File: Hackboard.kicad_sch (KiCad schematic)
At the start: 15 parts, among them SW1 SW_MEC_5E, U1 STM32L476RGT6

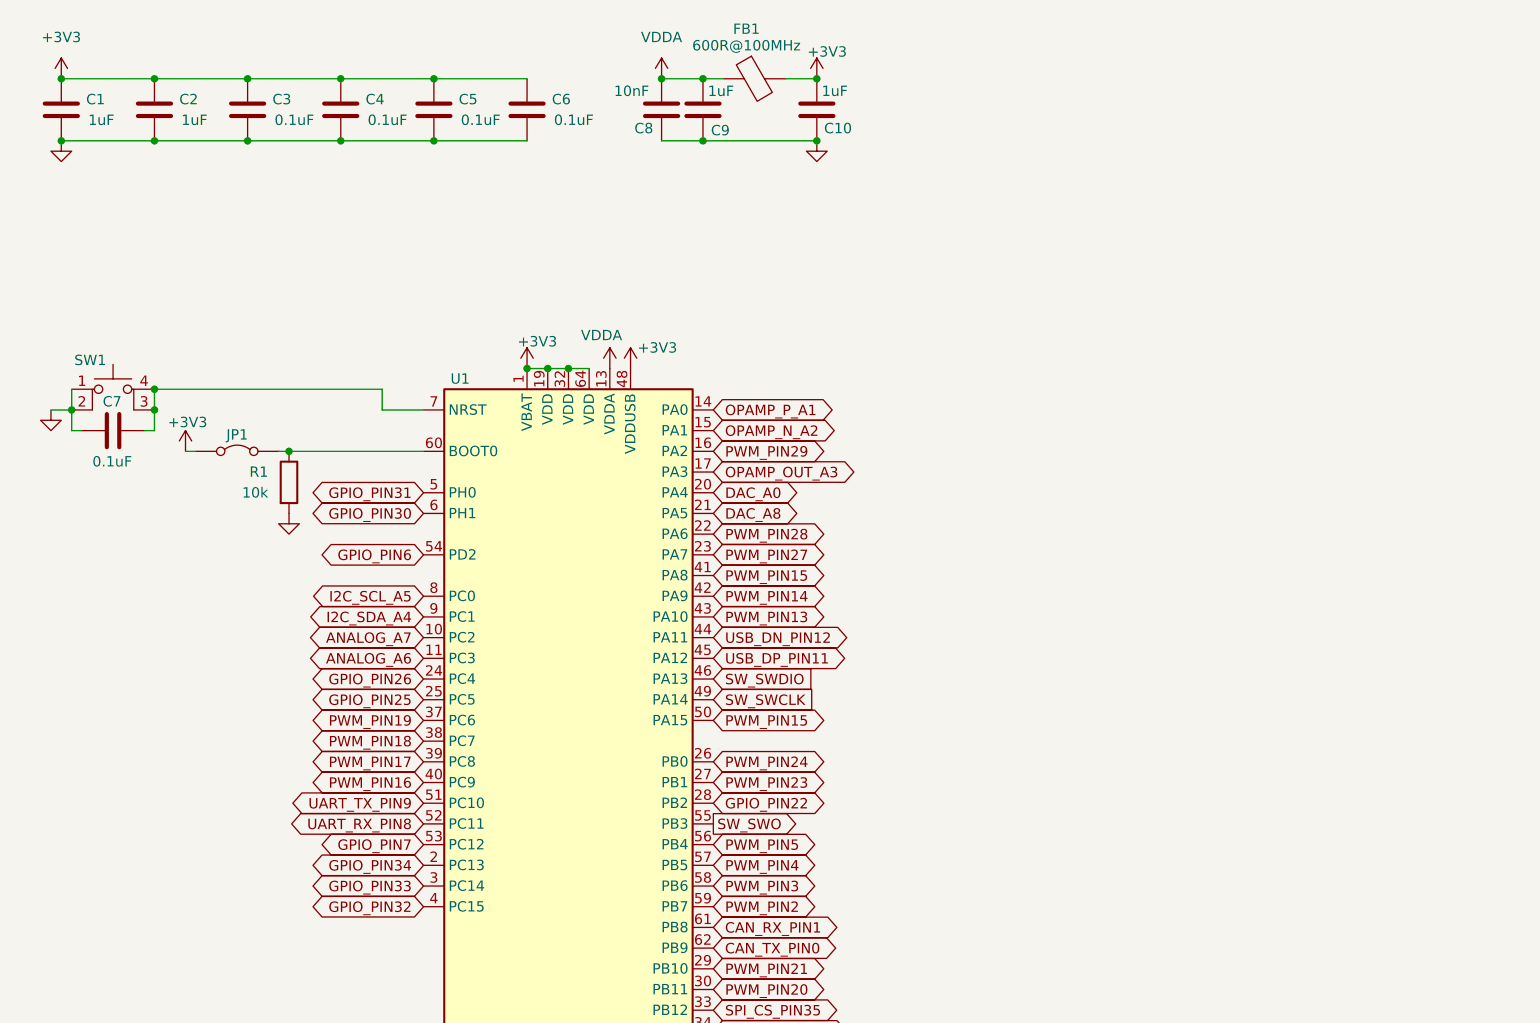
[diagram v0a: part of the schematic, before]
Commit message: Update README; Add power line and SPI for Micro SD
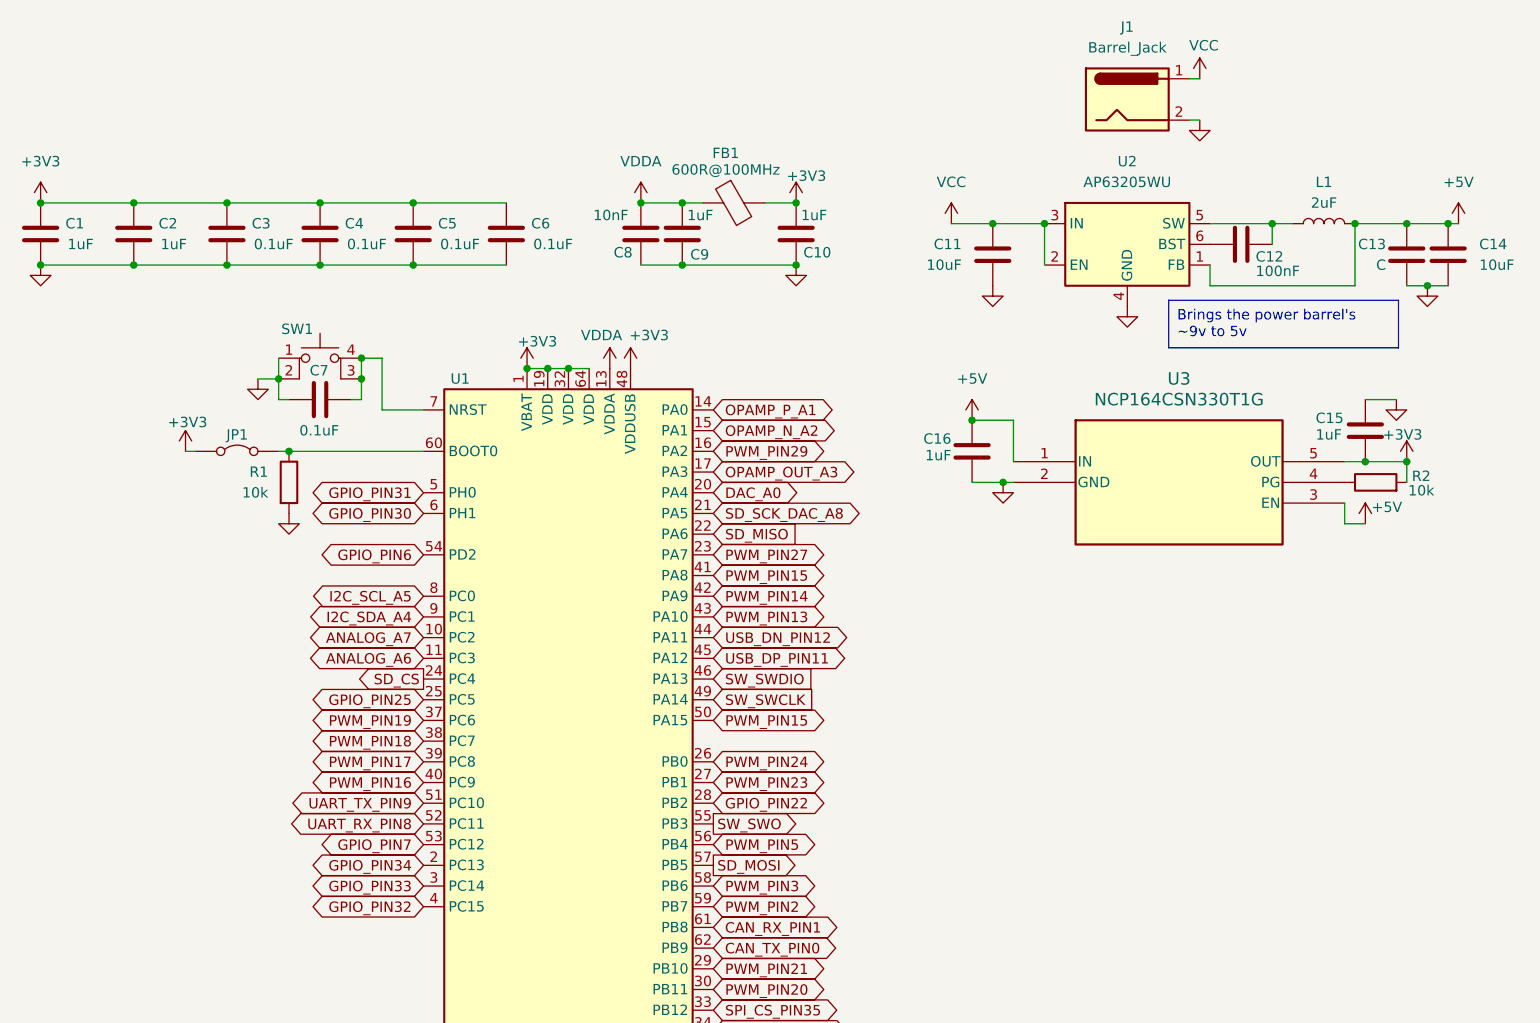
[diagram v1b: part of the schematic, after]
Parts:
- added C11, C14: 10uF, symbol Device:C
- added C12: 100nF, symbol Device:C
- added C13: C, symbol Device:C
- added C15, C16: 1uF, symbol Device:C
- added J1: Barrel_Jack, symbol Connector:Barrel_Jack
- added L1: 2uF, symbol Device:L
- added R2: 10k, symbol Device:R
- added U2: AP63205WU, Package_TO_SOT_SMD:TSOT-23-6, symbol Regulator_Switching:AP63205WU
- added U3: NCP164CSN330T1G, FP-NCP164CSN330T1G_OSI, symbol NCP164CSN:NCP164CSN330T1G
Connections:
- net +3V3: now also C15.2, R2.2, U3.5 (OUT)
- net GND: now also C11.2, C13.2, C14.2, C15.1, C16.2, J1.2, U2.4 (GND), U3.2 (GND)
- net DAC_A8 renamed SD_SCK_DAC_A8
- net GPIO_PIN26 renamed SD_CS
- net PWM_PIN28 renamed SD_MISO
- net PWM_PIN4 renamed SD_MOSI
- new net: C12.2, L1.1, U2.5 (SW)
- new net: R2.1, U3.4 (PG)
- new net: C12.1, U2.6 (BST)
- new net +5V: C13.1, C14.1, C16.1, L1.2, U2.1 (FB), U3.1 (IN), U3.3 (EN)
- new net VCC: C11.1, J1.1, U2.2 (EN), U2.3 (IN)
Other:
- moved on the sheet: C1, C10, C2, C3, C4, C5, C6, C7, C8, C9, FB1, SW1

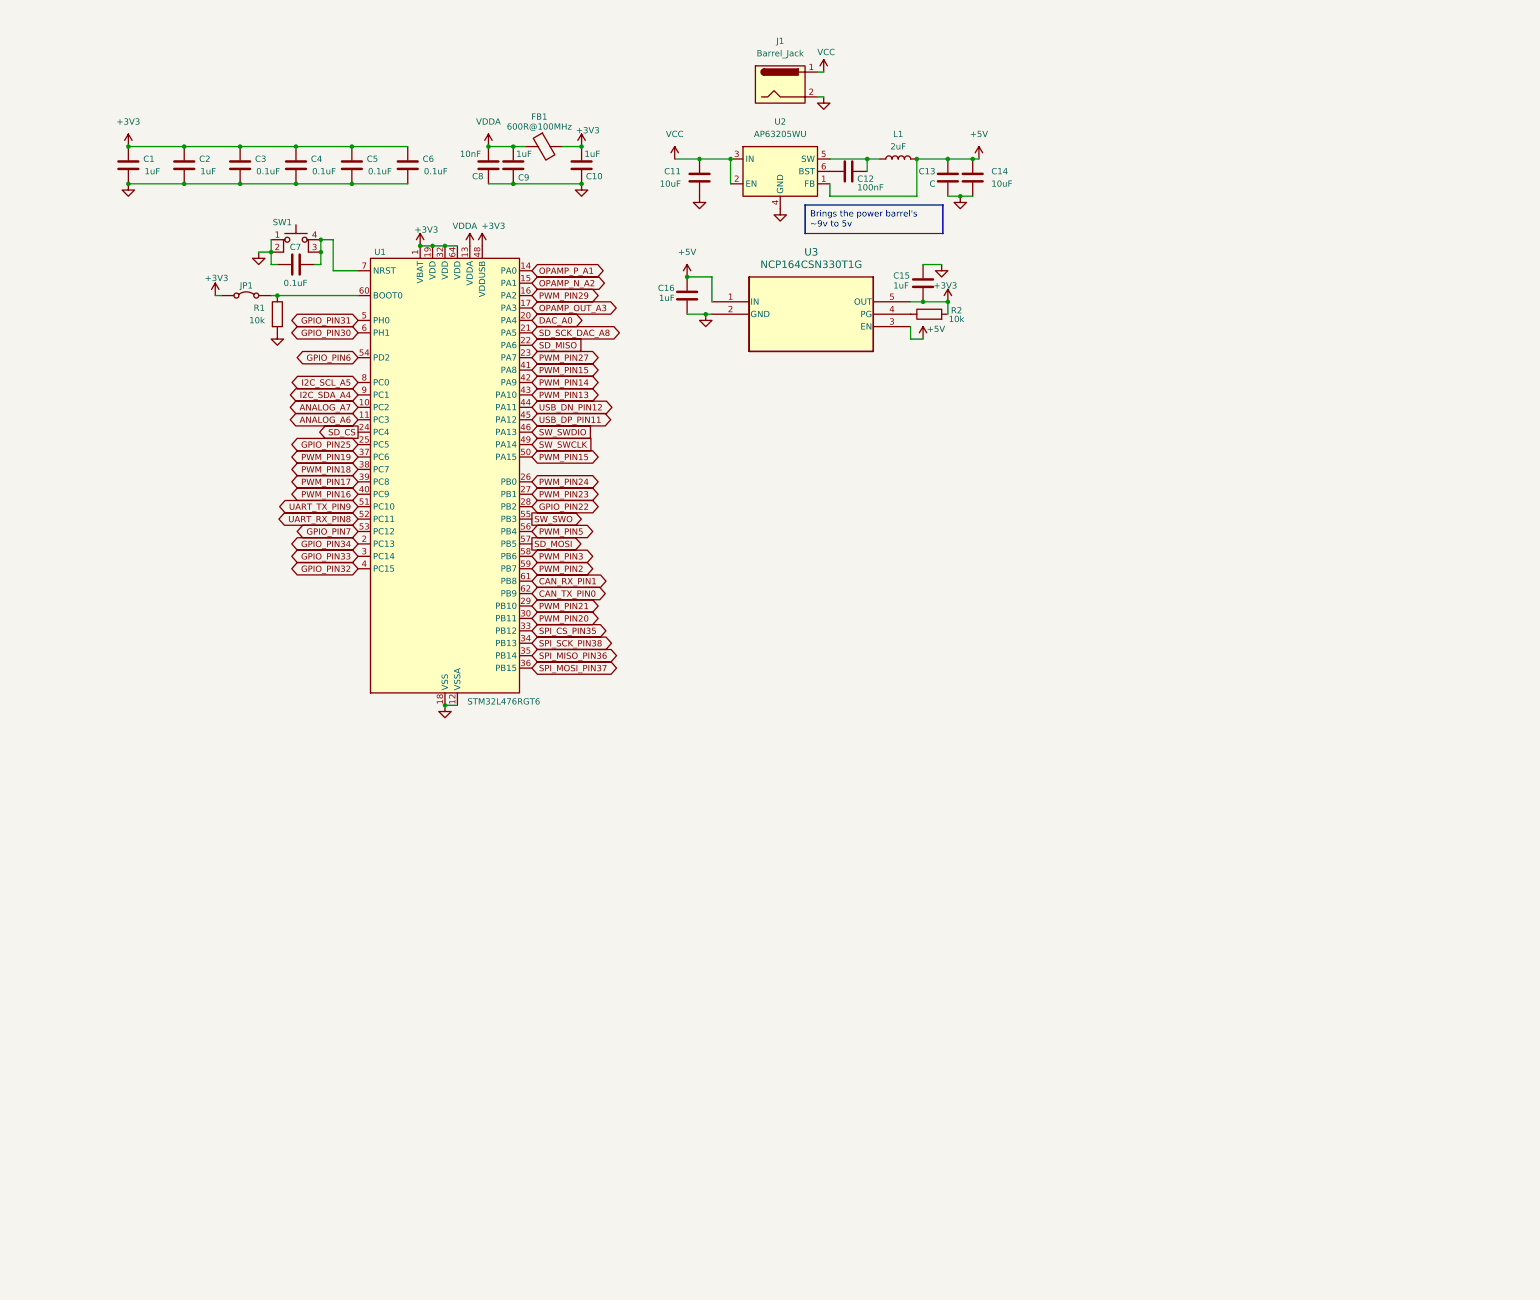
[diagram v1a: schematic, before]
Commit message: Add USB, SD Card, LED's and other small things
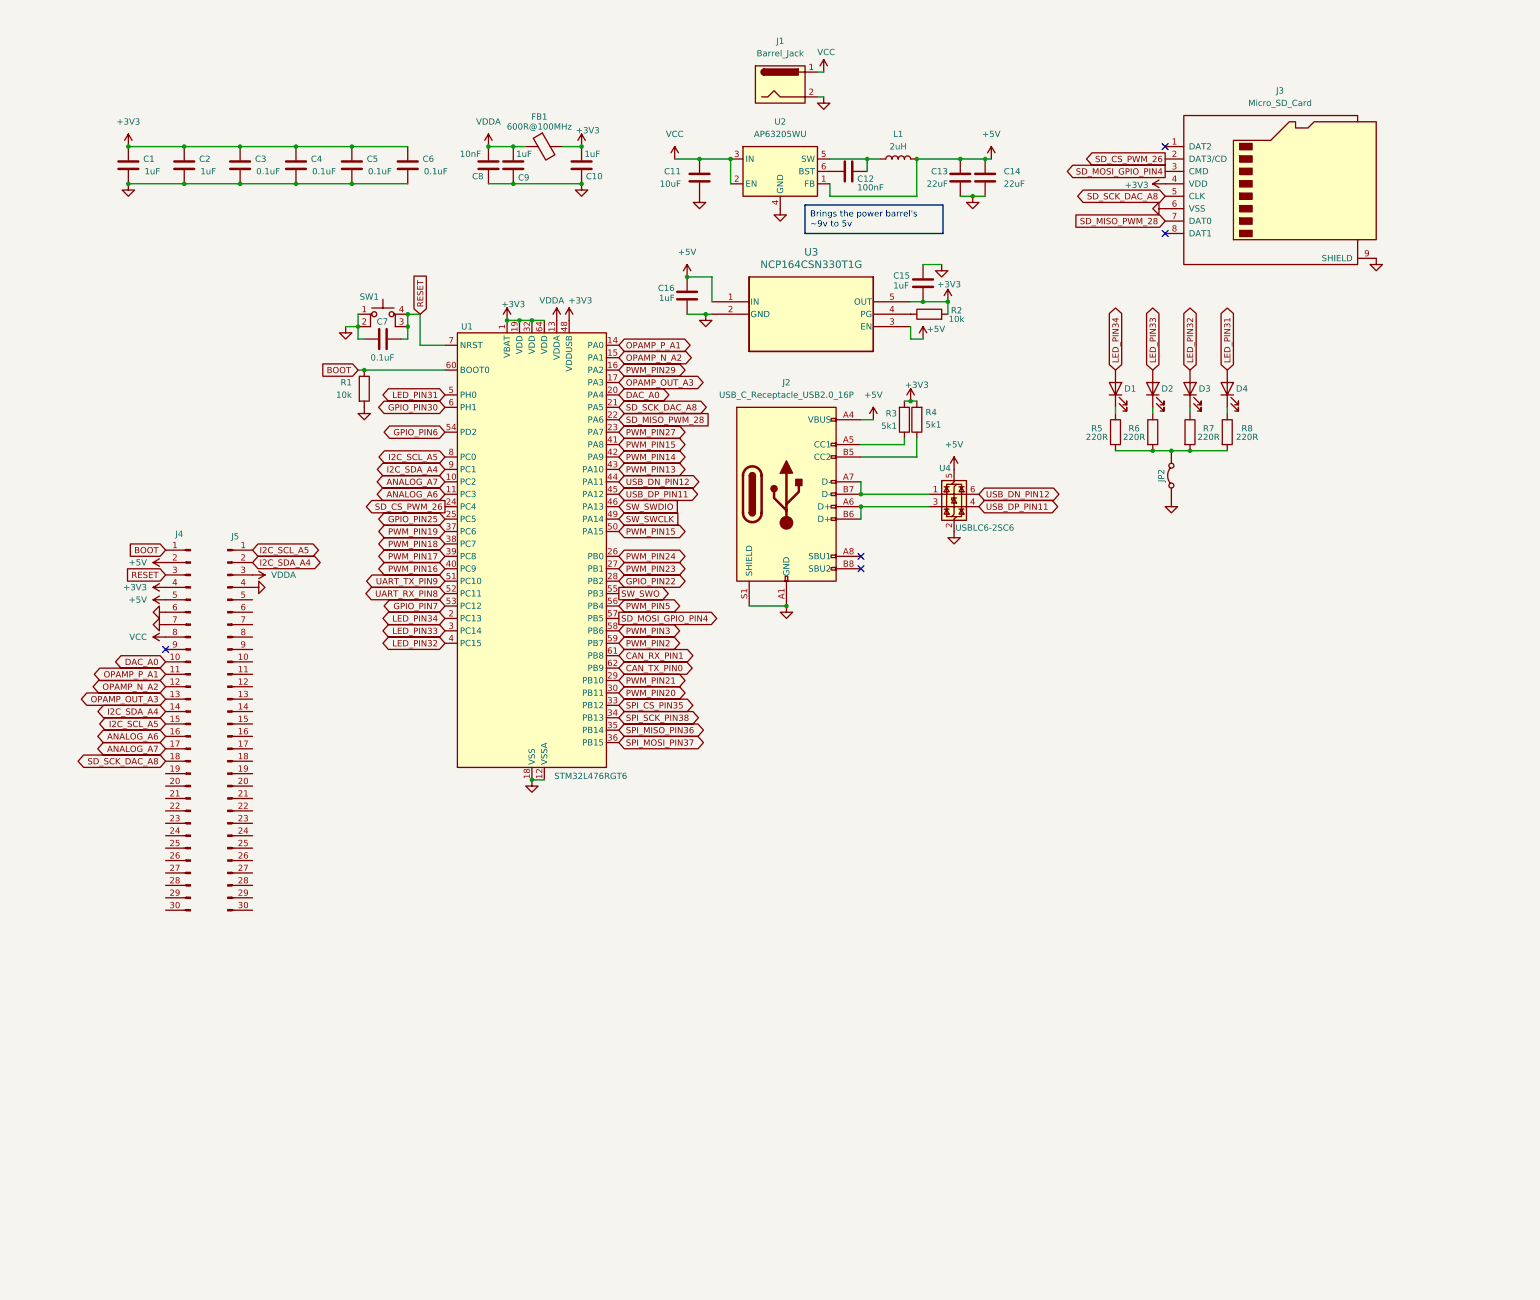
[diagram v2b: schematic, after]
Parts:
- removed JP1: Jumper_2_Bridged, symbol Jumper:Jumper_2_Bridged
- added D1, D2, D3, D4: LED, symbol Device:LED
- added J2: USB_C_Receptacle_USB2.0_16P, symbol Connector:USB_C_Receptacle_USB2.0_16P
- added J3: Micro_SD_Card, symbol Connector:Micro_SD_Card
- added J4, J5: Conn_01x30_Pin, symbol Connector:Conn_01x30_Pin
- added JP2: Jumper_2_Bridged, symbol Jumper:Jumper_2_Bridged
- added R3, R4: 5k1, symbol Device:R
- added R5, R6, R7, R8: 220R, symbol Device:R
- added U4: USBLC6-2SC6, Package_TO_SOT_SMD:SOT-23-6, symbol Power_Protection:USBLC6-2SC6
- C13: value C -> 22uF
- C14: value 10uF -> 22uF
- L1: value 2uF -> 2uH
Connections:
- net +3V3: now also J3.4 (VDD), J4.4 (Pin_4), R3.2, R4.2
- net +5V: now also J2.A4 (VBUS), J2.A9 (VBUS), J2.B4 (VBUS), J2.B9 (VBUS), J4.2 (Pin_2), J4.5 (Pin_5), U4.5 (VBUS)
- net ANALOG_A6: now also J4.16 (Pin_16)
- net ANALOG_A7: now also J4.17 (Pin_17)
- net DAC_A0: now also J4.10 (Pin_10)
- net GND: now also J2.A1 (GND), J2.A12 (GND), J2.B1 (GND), J2.B12 (GND), J2.S1 (SHIELD), J3.6 (VSS), J3.9 (SHIELD), J4.6 (Pin_6), J4.7 (Pin_7), J5.4 (Pin_4), JP2.1 (A), U4.2 (GND)
- net I2C_SCL_A5: now also J4.15 (Pin_15), J5.1 (Pin_1)
- net I2C_SDA_A4: now also J4.14 (Pin_14), J5.2 (Pin_2)
- net OPAMP_N_A2: now also J4.12 (Pin_12)
- net OPAMP_OUT_A3: now also J4.13 (Pin_13)
- net OPAMP_P_A1: now also J4.11 (Pin_11)
- net SD_SCK_DAC_A8: now also J3.5 (CLK), J4.18 (Pin_18)
- net USB_DN_PIN12: now also U4.6 (I/O1)
- net USB_DP_PIN11: now also U4.4 (I/O2)
- net VCC: now also J4.8 (Pin_8)
- net VDDA: now also J5.3 (Pin_3)
- net BOOT: now reaches R1.1, U1.60 (BOOT0)
- net BOOT: now also J4.1 (Pin_1)
- net RESET: now reaches C7.1, SW1.3 (K), SW1.4 (A), U1.7 (NRST)
- net RESET: now also J4.3 (Pin_3)
- net GPIO_PIN31 renamed LED_PIN31
- net LED_PIN31: now also D4.2 (A)
- net GPIO_PIN32 renamed LED_PIN32
- net LED_PIN32: now also D3.2 (A)
- net GPIO_PIN33 renamed LED_PIN33
- net LED_PIN33: now also D2.2 (A)
- net GPIO_PIN34 renamed LED_PIN34
- net LED_PIN34: now also D1.2 (A)
- net SD_CS renamed SD_CS_PWM_26
- net SD_CS_PWM_26: now also J3.2 (DAT3/CD)
- net SD_MISO renamed SD_MISO_PWM_28
- net SD_MISO_PWM_28: now also J3.7 (DAT0)
- net SD_MOSI renamed SD_MOSI_GPIO_PIN4
- net SD_MOSI_GPIO_PIN4: now also J3.3 (CMD)
- new net: D4.1 (K), R8.1
- new net: JP2.2 (B), R5.2, R6.2, R7.2, R8.2
- new net: D2.1 (K), R6.1
- new net: D1.1 (K), R5.1
- new net: D3.1 (K), R7.1
- new net: J2.A7 (D-), J2.B7 (D-), U4.1 (I/O1)
- new net: J2.A6 (D+), J2.B6 (D+), U4.3 (I/O2)
- new net: J2.A5 (CC1), R3.1
- new net: J2.B5 (CC2), R4.1
- no-connect marks 0 -> 5
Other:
- moved on the sheet: C13, C14, C7, R1, SW1, U1
